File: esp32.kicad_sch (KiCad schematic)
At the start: 5 parts, among them IC1 ESP32-S3-MINI-1U-N8, J4 USB_C_Receptacle_USB2.0, U15 USBLC6-2SC6

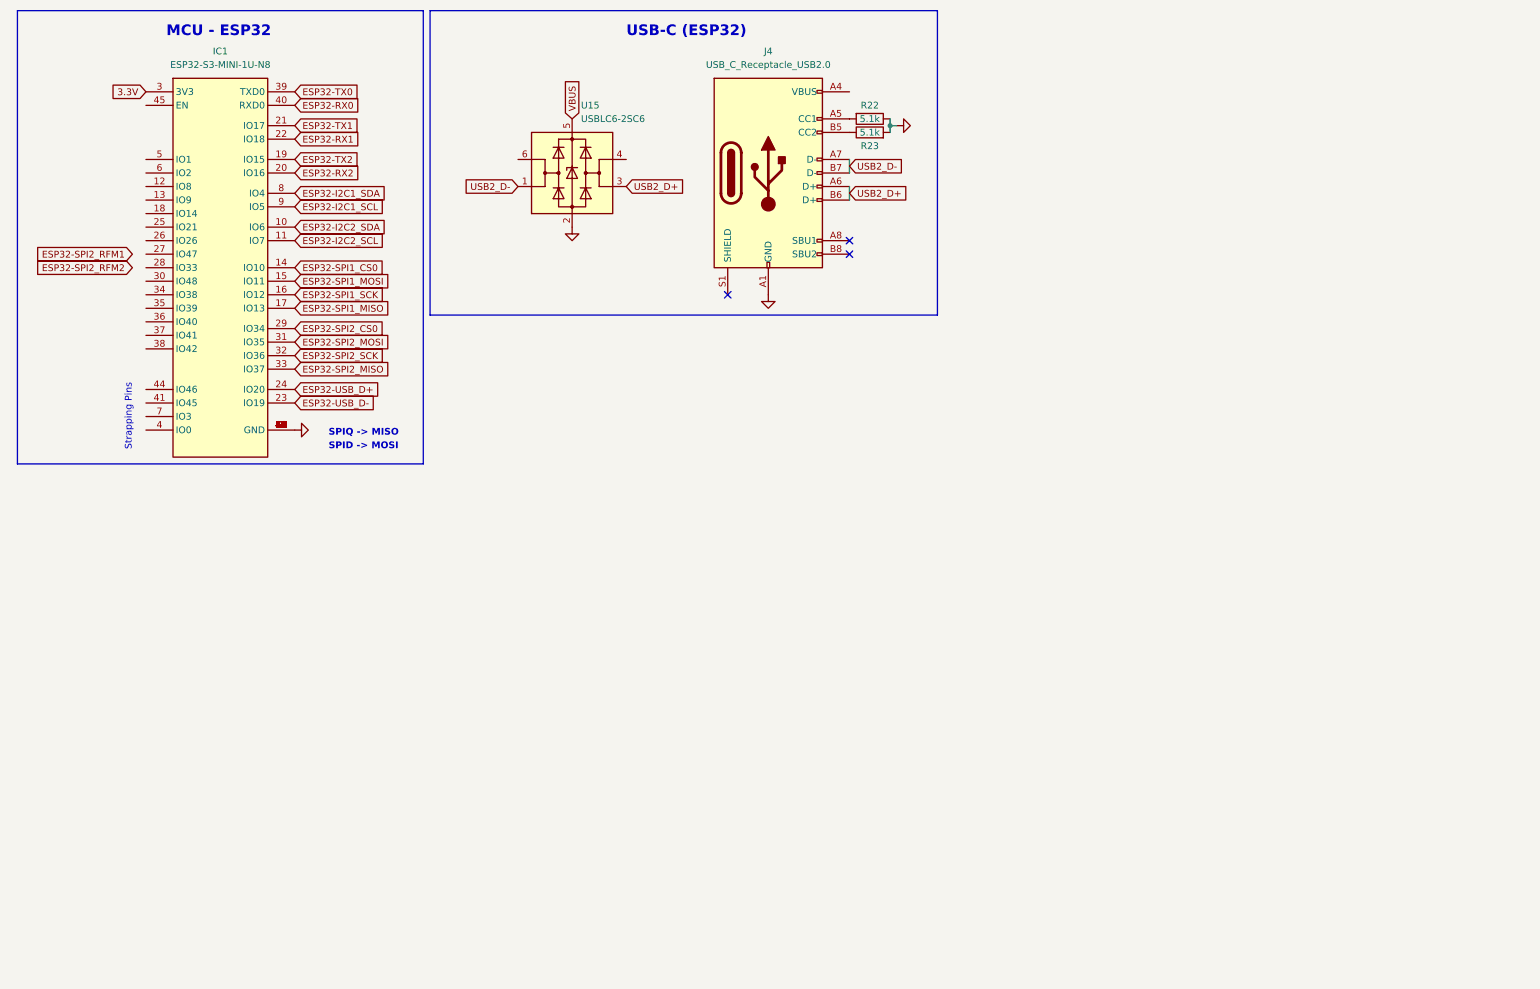
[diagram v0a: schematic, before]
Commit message: Organized Schematics & Fixed Notes
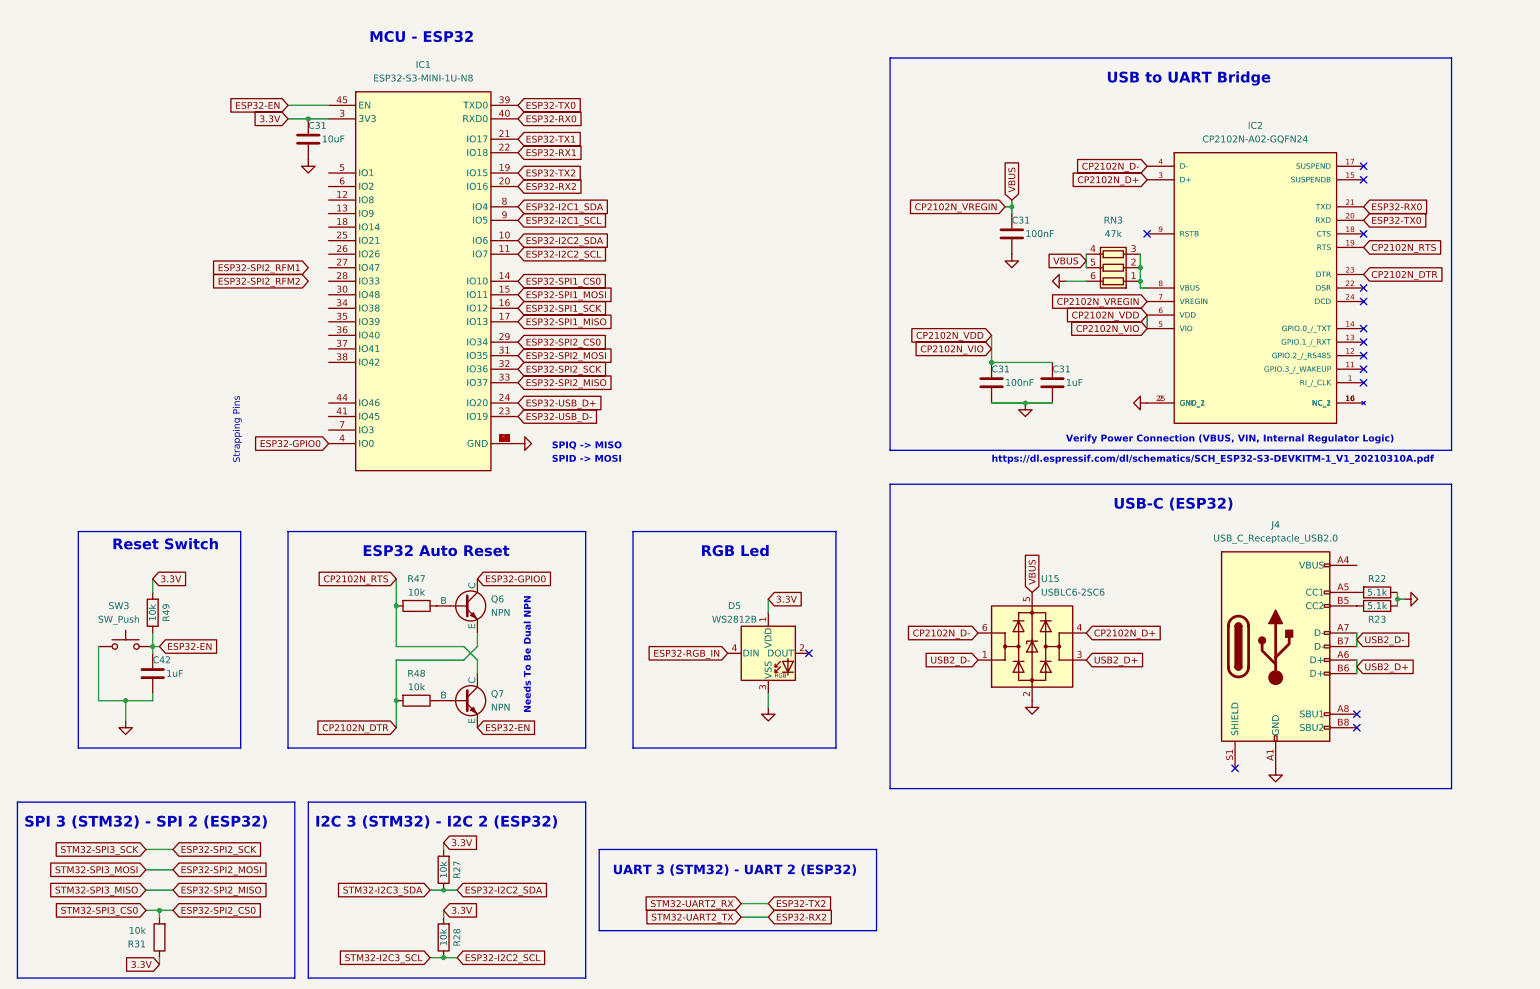
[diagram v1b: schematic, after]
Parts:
- added C31 (x2): 100nF, Capacitor_SMD:C_0201_0603Metric, symbol Device:C
- added C31: 10uF, Capacitor_SMD:C_0201_0603Metric, symbol Device:C
- added C31, C42: 1uF, Capacitor_SMD:C_0201_0603Metric, symbol Device:C
- added D5: WS2812B, LED_SMD:LED_WS2812B_PLCC4_5.0x5.0mm_P3.2mm, symbol LED:WS2812B
- added IC2: CP2102N-A02-GQFN24, QFN50P400X400X80-25N, symbol CP2102N-A02-GQFN24:CP2102N-A02-GQFN24
- added Q6, Q7: NPN, symbol Simulation_SPICE:NPN
- added R27, R28, R31: 10k, Resistor_SMD:R_0201_0603Metric, symbol Device:R
- added R47, R48, R49: 10k, symbol Device:R
- added RN3: 47k, symbol Device:R_Pack03
- added SW3: SW_Push, symbol Switch:SW_Push
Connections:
- net 3.3V: now also C31.1, D5.1 (VDD), R27.2, R28.2, R31.1, R49.2
- net ESP32-I2C2_SCL: now also R28.1
- net ESP32-I2C2_SDA: now also R27.1
- net ESP32-RX0: now also IC2.21 (TXD)
- net ESP32-SPI2_CS0: now also R31.2
- net ESP32-TX0: now also IC2.20 (RXD)
- net GND: now also C31.2, C31.2, C31.2, C31.2, C42.2, D5.3 (VSS), IC2.2 (GND_1), IC2.25 (GND_2), RN3.6 (R1.2), SW3.1
- net CP2102N_D+: now reaches U15.4 (I/O2)
- net CP2102N_D+: now also IC2.3 (D+)
- net CP2102N_D-: now reaches U15.6 (I/O1)
- net CP2102N_D-: now also IC2.4 (D-)
- net ESP32-GPIO0: now reaches IC1.4 (IO0)
- net ESP32-GPIO0: now also Q6.1 (C)
- net ESP32-EN: now reaches IC1.45 (EN)
- net ESP32-EN: now also C42.1, Q7.3 (E), R49.1, SW3.2
- net VBUS renamed CP2102N_VREGIN
- net CP2102N_VREGIN: now also C31.1, IC2.7 (VREGIN), RN3.4 (R3.2), RN3.5 (R2.2)
- new net: IC2.10 (NC_1), IC2.16 (NC_2)
- new net: IC2.8 (VBUS), RN3.1 (R1.1), RN3.2 (R2.1), RN3.3 (R3.1)
- new net: Q6.2 (B), R47.1
- new net: Q7.2 (B), R48.1
- new net CP2102N_DTR: IC2.23 (DTR), Q6.3 (E), R48.2
- new net CP2102N_RTS: IC2.19 (RTS), Q7.1 (C), R47.2
- new net CP2102N_VDD: C31.1, C31.1, IC2.5 (VIO), IC2.6 (VDD)
- new net ESP32-RGB_IN: D5.4 (DIN)
- no-connect marks 3 -> 15
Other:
- note added: "ESP32 Auto Reset"
- note added: "I2C 3 (STM32) - I2C 2 (ESP32)"
- note added: "Needs To Be Dual NPN"
- note added: "RGB Led"
- note added: "Reset Switch"
- note added: "SPI 3 (STM32) - SPI 2 (ESP32)"
- note added: "UART 3 (STM32) - UART 2 (ESP32)"
- note added: "USB to UART Bridge"
- note added: "Verify Power Connection (VBUS, VIN, Internal Regulator Logic)"
- note added: "https://dl.espressif.com/dl/schematics/SCH_ESP32-S3-DEVKITM-1_V1_20210310A.pdf"
- company: (none) -> nyuad.space
- title: (none) -> MCU - ESP32 Schematic
- moved on the sheet: IC1, J4, R22, R23, U15

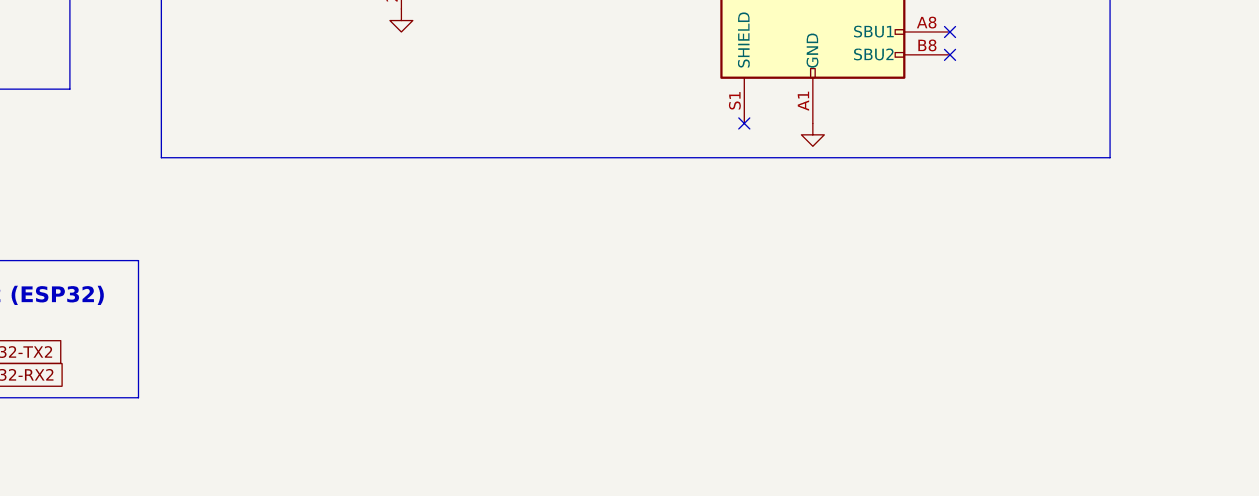
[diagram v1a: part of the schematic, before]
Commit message: Added OSH Logo
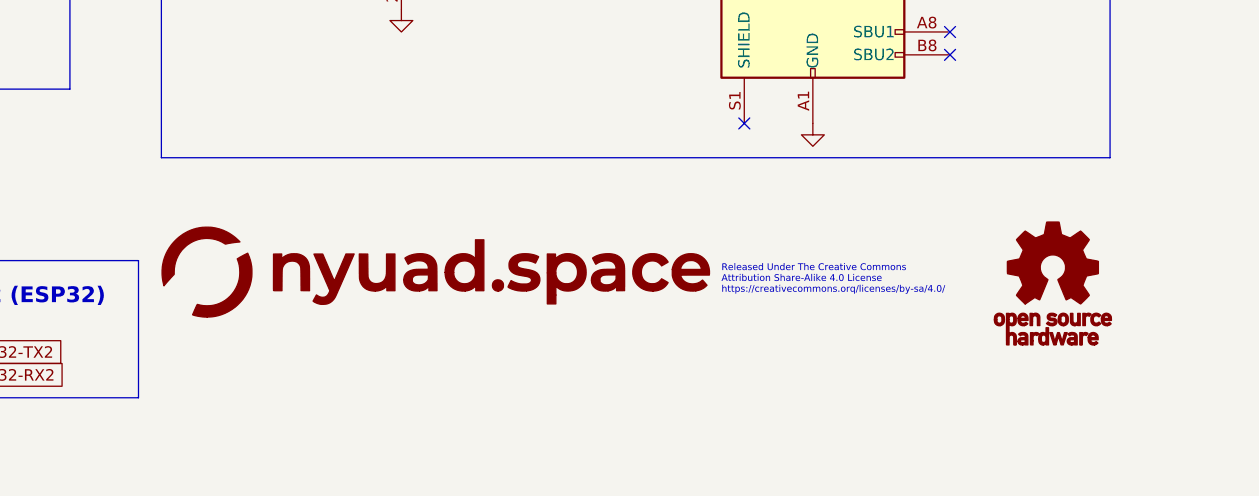
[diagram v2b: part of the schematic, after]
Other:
- note added: "Released Under The Creative Commons Attribution Share-Alike 4.0 License https://creativecommons.orq/licenses/by-sa/4.0/"
- company: nyuad.space -> Aether Flight Computer
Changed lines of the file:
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@@
   (title_block
     (title "MCU - ESP32 Schematic")
-    (company "nyuad.space")
-    (comment 1 "Aether Flight Computer")
+    (company "Aether Flight Computer")
+    (comment 7 "Aether Flight Computer")
   )
   (junction (at 85.09 143.51) (diameter 0) (color 0 0 0 0)
@@
   (text "Reset Switch" (at 31.75 115.57 0)
     (effects (font (size 2 2) (thickness 0.8) bold) (justify left bottom))
+  )
+  (text "Released Under The Creative Commons\nAttribution Share-Alike 4.0 License\nhttps://creativecommons.orq/licenses/by-sa/4.0/"
+    (at 240.03 175.26 0)
+    (effects (font (face "KiCad Font") (size 0.75 0.75)) (justify left bottom))
   )
   (text "SPIQ -> MISO" (at 114.3 96.52 0)
@@
     )
   )
+  (symbol (lib_id "osh_logo:LOGO") (at 276.86 173.99 0) (unit 1)
+    (in_bom yes) (on_board yes) (dnp no) (fields_autoplaced)
+    (property "Reference" "#G1" (at 276.86 167.7874 0)
+      (effects (font (size 1.27 1.27)) hide)
+    )
+    (property "Value" "LOGO" (at 276.86 180.1926 0)
+      (effects (font (size 1.27 1.27)) hide)
+    )
+    (property "Footprint" "" (at 276.86 173.99 0)
+      (effects (font (size 1.27 1.27)) hide)
+    )
+    (property "Datasheet" "" (at 276.86 173.99 0)
+      (effects (font (size 1.27 1.27)) hide)
+    )
+    (instances
+      (project "aether"
+        (path "/e12346fa-509d-4de9-8ab1-dced307292db"
+          (reference "#G1") (unit 1)
+        )
+        (path "/e12346fa-509d-4de9-8ab1-dced307292db/a5bc5271-f6b1-46bc-807d-d0d88ce9901f"
+          (reference "#G4") (unit 1)
+        )
+      )
+    )
+  )
   (symbol (lib_id "Device:C") (at 208.28 83.82 0) (unit 1)
     (in_bom yes) (on_board yes) (dnp no)
@@
         )
       )
+    )
+  )
+  (symbol (lib_id "nyuad_space:LOGO") (at 208.28 172.72 0) (unit 1)
+    (in_bom yes) (on_board yes) (dnp no) (fields_autoplaced)
+    (property "Reference" "#G2" (at 208.28 168.3609 0)
+      (effects (font (size 1.27 1.27)) hide)
+    )
+    (property "Value" "LOGO" (at 208.28 177.0791 0)
+      (effects (font (size 1.27 1.27)) hide)
+    )
+    (property "Footprint" "" (at 208.28 172.72 0)
+      (effects (font (size 1.27 1.27)) hide)
+    )
+    (property "Datasheet" "" (at 208.28 172.72 0)
+      (effects (font (size 1.27 1.27)) hide)
+    )
+    (instances
+      (project "aether"
+        (path "/e12346fa-509d-4de9-8ab1-dced307292db"
+          (reference "#G2") (unit 1)
+        )
+        (path "/e12346fa-509d-4de9-8ab1-dced307292db/a5bc5271-f6b1-46bc-807d-d0d88ce9901f"
+          (reference "#G3") (unit 1)
+        )
+      )

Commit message: Updated files
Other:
- note removed: "Released Under The Creative Commons Attribution Share-Alike 4.0 License https://creativecommons.orq/licenses/by-sa/4.0/"
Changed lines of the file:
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@@
     (effects (font (size 2 2) (thickness 0.8) bold) (justify left bottom))
-  )
-  (text "Released Under The Creative Commons\nAttribution Share-Alike 4.0 License\nhttps://creativecommons.orq/licenses/by-sa/4.0/"
-    (at 240.03 175.26 0)
-    (effects (font (face "KiCad Font") (size 0.75 0.75)) (justify left bottom))
   )
   (text "SPIQ -> MISO" (at 114.3 96.52 0)
@@
     )
   )
-  (global_label "STM32-UART2_RX" (shape input) (at 149.86 181.61 180) (fields_autoplaced)
+  (global_label "STM32-UART3_RX" (shape input) (at 149.86 181.61 180) (fields_autoplaced)
     (effects (font (size 1.27 1.27)) (justify right))
     (property "Intersheetrefs" "${INTERSHEET_REFS}" (at 129.9416 181.61 0)
@@
     )
   )
-  (global_label "ESP32-SPI2_RFM2" (shape input) (at 68.58 64.77 180) (fields_autoplaced)
-    (effects (font (size 1.27 1.27)) (justify right))
-    (property "Intersheetrefs" "${INTERSHEET_REFS}" (at 47.694 64.77 0)
-      (effects (font (size 1.27 1.27)) (justify right) hide)
-    )
-  )
   (global_label "ESP32-I2C2_SCL" (shape input) (at 107.95 59.69 0) (fields_autoplaced)
     (effects (font (size 1.27 1.27)) (justify left))
@@
     )
   )
-  (global_label "ESP32-SPI2_RFM1" (shape input) (at 68.58 62.23 180) (fields_autoplaced)
-    (effects (font (size 1.27 1.27)) (justify right))
-    (property "Intersheetrefs" "${INTERSHEET_REFS}" (at 47.694 62.23 0)
-      (effects (font (size 1.27 1.27)) (justify right) hide)
-    )
-  )
   (global_label "ESP32-SPI2_MOSI" (shape input) (at 43.18 175.26 0) (fields_autoplaced)
     (effects (font (size 1.27 1.27)) (justify left))
@@
     )
   )
-  (global_label "STM32-UART2_TX" (shape input) (at 149.86 184.15 180) (fields_autoplaced)
+  (global_label "STM32-UART3_TX" (shape input) (at 149.86 184.15 180) (fields_autoplaced)
     (effects (font (size 1.27 1.27)) (justify right))
     (property "Intersheetrefs" "${INTERSHEET_REFS}" (at 130.244 184.15 0)
